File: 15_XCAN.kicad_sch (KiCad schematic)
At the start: 16 parts

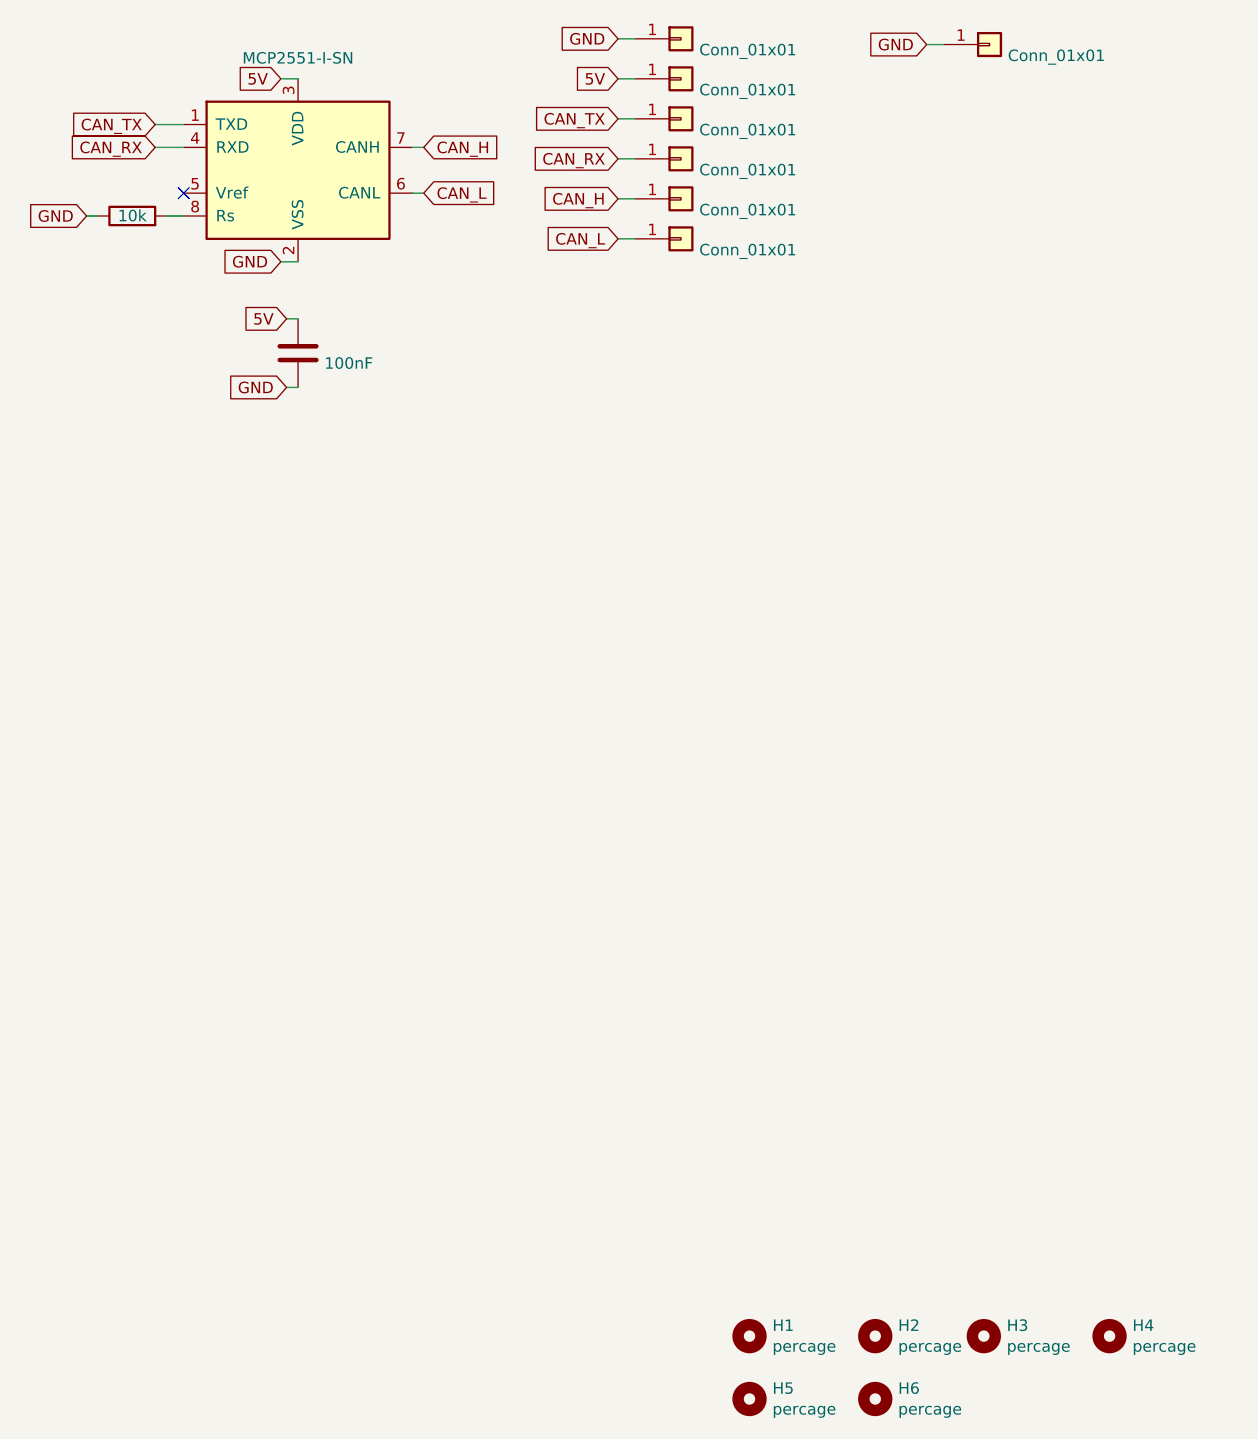
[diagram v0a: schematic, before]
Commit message: réduction de taille du pcb
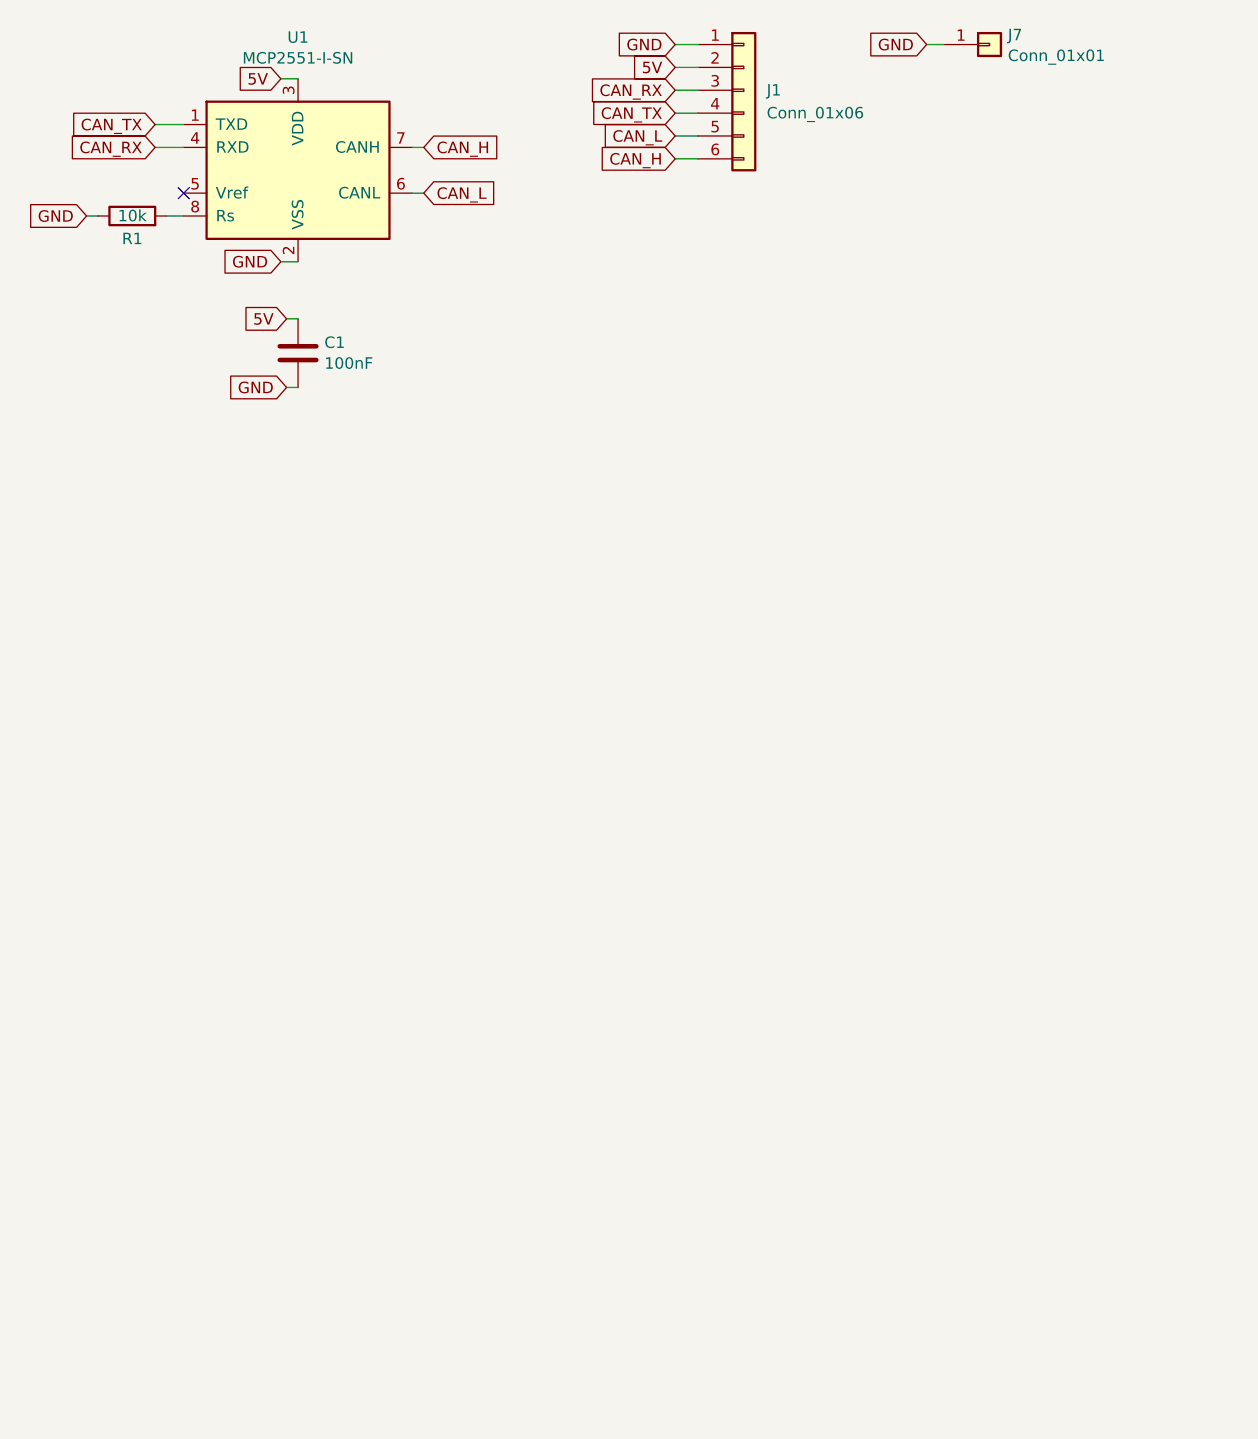
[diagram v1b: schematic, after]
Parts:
- removed ? (x6): Conn_01x01, Chimere_mods:Castellated_conn, symbol Connector_Generic:Conn_01x01
- removed H1, H2, H3, H4, H5, H6: percage, Chimere_comps:trou, symbol Mechanical:MountingHole
- added J1: Conn_01x06, Connector_PinHeader_2.54mm:PinHeader_1x06_P2.54mm_Vertical, symbol Connector_Generic:Conn_01x06
- J7: renamed from ?; footprint Chimere_mods:Castellated_conn -> Connector_PinHeader_2.54mm:PinHeader_1x01_P2.54mm_Vertical
- gave numbers to parts that had none: 3
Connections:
- net 5V: now also J1.2 (Pin_2)
- net CAN_H: now also J1.6 (Pin_6)
- net CAN_L: now also J1.5 (Pin_5)
- net CAN_RX: now also J1.3 (Pin_3)
- net CAN_TX: now also J1.4 (Pin_4)
- net GND: now also J1.1 (Pin_1)

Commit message: maj fichiers de fabrication
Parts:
- C1: LCSC (none) -> C14663
- U1: LCSC (none) -> C7376
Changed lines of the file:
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@@
       (effects (font (size 1.27 1.27) italic) hide)
     )
-    (property "Datasheet" "C7376" (id 3) (at 63.5 46.99 0)
+    (property "Datasheet" "-" (id 3) (at 63.5 46.99 0)
       (effects (font (size 1.27 1.27)) hide)
     )
+    (property "LCSC" "C7376" (id 4) (at 63.5 46.99 0))
     (pin "1")
     (pin "2")
@@
       (effects (font (size 1.27 1.27)) hide)
     )
-    (property "Datasheet" "C14663" (id 3) (at 63.5 67.31 0)
+    (property "Datasheet" "-" (id 3) (at 63.5 67.31 0)
       (effects (font (size 1.27 1.27)) hide)
     )
+    (property "LCSC" "C14663" (id 4) (at 63.5 67.31 0))
     (pin "1")
     (pin "2")

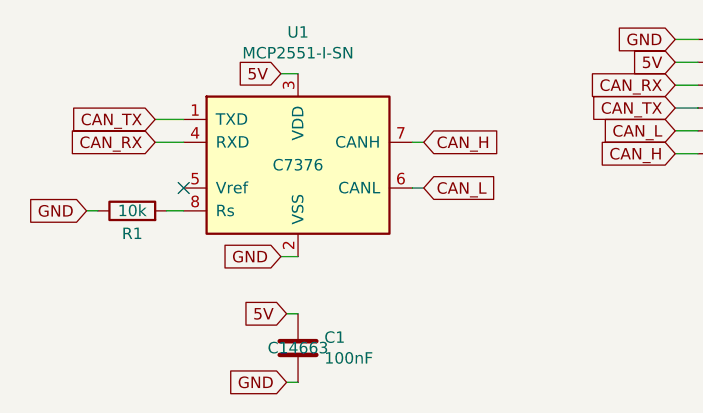
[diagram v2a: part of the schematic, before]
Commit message: maj
ajout sur silk
changement sourcing jlcpcb
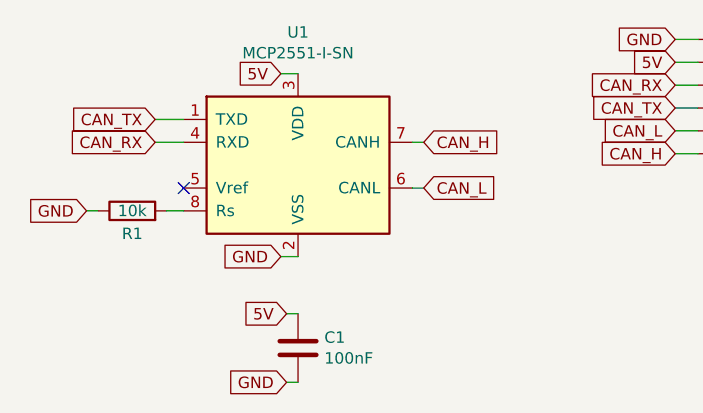
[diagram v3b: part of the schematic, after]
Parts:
- R1: LCSC (none) -> C25804
- U1: LCSC C7376 -> C49558
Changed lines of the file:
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@@
       (effects (font (size 1.27 1.27)) hide)
     )
-    (property "Datasheet" "C25804" (id 3) (at 45.085 52.07 0)
+    (property "Datasheet" "~" (id 3) (at 45.085 52.07 0)
+      (effects (font (size 1.27 1.27)) hide)
+    )
+    (property "LCSC" "C25804" (id 4) (at 45.085 52.07 90)
       (effects (font (size 1.27 1.27)) hide)
     )
@@
       (effects (font (size 1.27 1.27) italic) hide)
     )
-    (property "Datasheet" "-" (id 3) (at 63.5 46.99 0)
+    (property "Datasheet" "http://ww1.microchip.com/downloads/en/devicedoc/21667d.pdf" (id 3) (at 63.5 46.99 0)
       (effects (font (size 1.27 1.27)) hide)
     )
-    (property "LCSC" "C7376" (id 4) (at 63.5 46.99 0))
+    (property "LCSC" "C49558" (id 4) (at 63.5 46.99 0)
+      (effects (font (size 1.27 1.27)) hide)
+    )
     (pin "1")
     (pin "2")
@@
       (effects (font (size 1.27 1.27)) hide)
     )
-    (property "Datasheet" "-" (id 3) (at 63.5 67.31 0)
+    (property "Datasheet" "~" (id 3) (at 63.5 67.31 0)
       (effects (font (size 1.27 1.27)) hide)
     )
-    (property "LCSC" "C14663" (id 4) (at 63.5 67.31 0))
+    (property "LCSC" "C14663" (id 4) (at 63.5 67.31 0)
+      (effects (font (size 1.27 1.27)) hide)
+    )
     (pin "1")
     (pin "2")

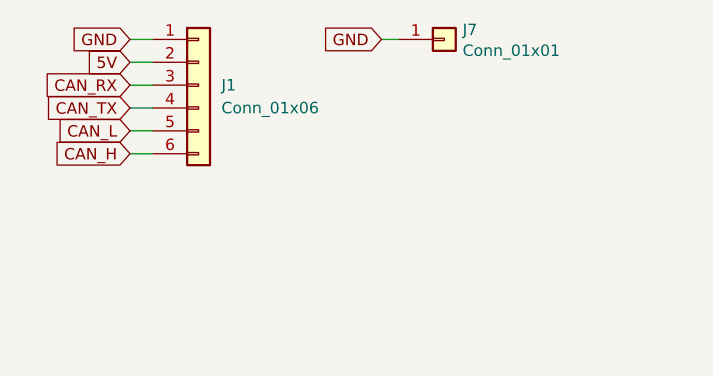
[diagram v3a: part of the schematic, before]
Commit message: version castellated holes
rajout des castellated holes
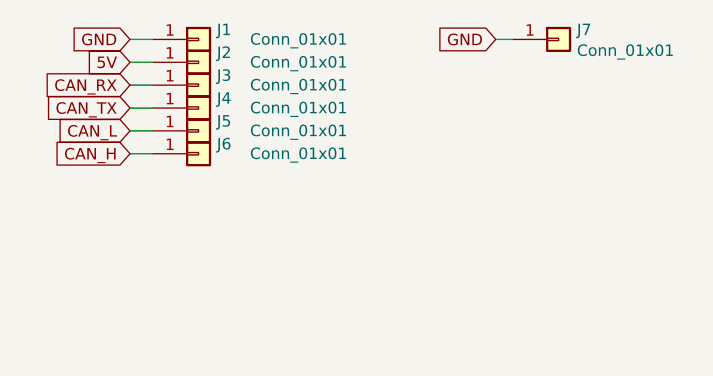
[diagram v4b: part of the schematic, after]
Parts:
- removed J1: Conn_01x06, Connector_PinHeader_2.54mm:PinHeader_1x06_P2.54mm_Vertical, symbol Connector_Generic:Conn_01x06
- added J1, J2, J3, J4, J5, J6: Conn_01x01, Chimere_mods:Castellated_conn, symbol Connector_Generic:Conn_01x01
- J7: footprint Connector_PinHeader_2.54mm:PinHeader_1x01_P2.54mm_Vertical -> Chimere_mods:Cast_co_1_905
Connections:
- net 5V: now also J2.1 (Pin_1)
- net CAN_H: now also J6.1 (Pin_1)
- net CAN_L: now also J5.1 (Pin_1)
- net CAN_RX: now also J3.1 (Pin_1)
- net CAN_TX: now also J4.1 (Pin_1)
- net GND: now also J1.1 (Pin_1)
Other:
- moved on the sheet: J7
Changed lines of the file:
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@@
     (stroke (width 0) (type default) (color 0 0 0 0))
   )
-  (wire (pts (xy 133.35 33.02) (xy 135.255 33.02))
+  (wire (pts (xy 146.05 33.02) (xy 147.955 33.02))
     (stroke (width 0) (type default) (color 0 0 0 0))
   )
@@
     )
   )
-  (global_label "GND" (shape input) (at 133.35 33.02 180) (fields_autoplaced)
-    (effects (font (size 1.27 1.27)) (justify right))
-    (property "Intersheet References" "${INTERSHEET_REFS}" (id 0) (at 0 0 0)
+  (global_label "GND" (shape input) (at 146.05 33.02 180) (fields_autoplaced)
+    (effects (font (size 1.27 1.27)) (justify right))
+    (property "Intersheet References" "${INTERSHEET_REFS}" (id 0) (at 12.7 0 0)
       (effects (font (size 1.27 1.27)) hide)
     )
@@
     (pin "2")
   )
-  (symbol (lib_id "Connector_Generic:Conn_01x01") (at 140.335 33.02 0) (unit 1)
-    (in_bom yes) (on_board yes)
-    (property "Reference" "J7" (id 0) (at 142.367 31.9532 0)
-      (effects (font (size 1.27 1.27)) (justify left))
-    )
-    (property "Value" "Conn_01x01" (id 1) (at 142.367 34.2646 0)
-      (effects (font (size 1.27 1.27)) (justify left))
-    )
-    (property "Footprint" "Connector_PinHeader_2.54mm:PinHeader_1x01_P2.54mm_Vertical" (id 2) (at 140.335 33.02 0)
-      (effects (font (size 1.27 1.27)) hide)
-    )
-    (property "Datasheet" "~" (id 3) (at 140.335 33.02 0)
-      (effects (font (size 1.27 1.27)) hide)
-    )
-    (pin "1")
-  )
-  (symbol (lib_id "Connector_Generic:Conn_01x06") (at 113.03 38.1 0) (unit 1)
-    (in_bom yes) (on_board yes) (fields_autoplaced)
-    (property "Reference" "J1" (id 0) (at 115.57 38.0999 0)
-      (effects (font (size 1.27 1.27)) (justify left))
-    )
-    (property "Value" "Conn_01x06" (id 1) (at 115.57 40.6399 0)
-      (effects (font (size 1.27 1.27)) (justify left))
-    )
-    (property "Footprint" "Connector_PinHeader_2.54mm:PinHeader_1x06_P2.54mm_Vertical" (id 2) (at 113.03 38.1 0)
+  (symbol (lib_id "Connector_Generic:Conn_01x01") (at 153.035 33.02 0) (unit 1)
+    (in_bom yes) (on_board yes)
+    (property "Reference" "J7" (id 0) (at 155.067 31.9532 0)
+      (effects (font (size 1.27 1.27)) (justify left))
+    )
+    (property "Value" "Conn_01x01" (id 1) (at 155.067 34.2646 0)
+      (effects (font (size 1.27 1.27)) (justify left))
+    )
+    (property "Footprint" "Chimere_mods:Cast_co_1_905" (id 2) (at 153.035 33.02 0)
+      (effects (font (size 1.27 1.27)) hide)
+    )
+    (property "Datasheet" "~" (id 3) (at 153.035 33.02 0)
+      (effects (font (size 1.27 1.27)) hide)
+    )
+    (pin "1")
+  )
+  (symbol (lib_id "Connector_Generic:Conn_01x01") (at 113.03 33.02 0) (unit 1)
+    (in_bom yes) (on_board yes)
+    (property "Reference" "J1" (id 0) (at 115.062 31.9532 0)
+      (effects (font (size 1.27 1.27)) (justify left))
+    )
+    (property "Value" "Conn_01x01" (id 1) (at 118.745 33.02 0)
+      (effects (font (size 1.27 1.27)) (justify left))
+    )
+    (property "Footprint" "Chimere_mods:Castellated_conn" (id 2) (at 113.03 33.02 0)
+      (effects (font (size 1.27 1.27)) hide)
+    )
+    (property "Datasheet" "~" (id 3) (at 113.03 33.02 0)
+      (effects (font (size 1.27 1.27)) hide)
+    )
+    (pin "1")
+  )
+  (symbol (lib_id "Connector_Generic:Conn_01x01") (at 113.03 45.72 0) (unit 1)
+    (in_bom yes) (on_board yes)
+    (property "Reference" "J6" (id 0) (at 115.062 44.6532 0)
+      (effects (font (size 1.27 1.27)) (justify left))
+    )
+    (property "Value" "Conn_01x01" (id 1) (at 118.745 45.72 0)
+      (effects (font (size 1.27 1.27)) (justify left))
+    )
+    (property "Footprint" "Chimere_mods:Castellated_conn" (id 2) (at 113.03 45.72 0)
+      (effects (font (size 1.27 1.27)) hide)
+    )
+    (property "Datasheet" "~" (id 3) (at 113.03 45.72 0)
+      (effects (font (size 1.27 1.27)) hide)
+    )
+    (pin "1")
+  )
+  (symbol (lib_id "Connector_Generic:Conn_01x01") (at 113.03 35.56 0) (unit 1)
+    (in_bom yes) (on_board yes)
+    (property "Reference" "J2" (id 0) (at 115.062 34.4932 0)
+      (effects (font (size 1.27 1.27)) (justify left))
+    )
+    (property "Value" "Conn_01x01" (id 1) (at 118.745 35.56 0)
+      (effects (font (size 1.27 1.27)) (justify left))
+    )
+    (property "Footprint" "Chimere_mods:Castellated_conn" (id 2) (at 113.03 35.56 0)
+      (effects (font (size 1.27 1.27)) hide)
+    )
+    (property "Datasheet" "~" (id 3) (at 113.03 35.56 0)
+      (effects (font (size 1.27 1.27)) hide)
+    )
+    (pin "1")
+  )
+  (symbol (lib_id "Connector_Generic:Conn_01x01") (at 113.03 40.64 0) (unit 1)
+    (in_bom yes) (on_board yes)
+    (property "Reference" "J4" (id 0) (at 115.062 39.5732 0)
+      (effects (font (size 1.27 1.27)) (justify left))
+    )
+    (property "Value" "Conn_01x01" (id 1) (at 118.745 40.64 0)
+      (effects (font (size 1.27 1.27)) (justify left))
+    )
+    (property "Footprint" "Chimere_mods:Castellated_conn" (id 2) (at 113.03 40.64 0)
+      (effects (font (size 1.27 1.27)) hide)
+    )
+    (property "Datasheet" "~" (id 3) (at 113.03 40.64 0)
+      (effects (font (size 1.27 1.27)) hide)
+    )
+    (pin "1")
+  )
+  (symbol (lib_id "Connector_Generic:Conn_01x01") (at 113.03 38.1 0) (unit 1)
+    (in_bom yes) (on_board yes)
+    (property "Reference" "J3" (id 0) (at 115.062 37.0332 0)
+      (effects (font (size 1.27 1.27)) (justify left))
+    )
+    (property "Value" "Conn_01x01" (id 1) (at 118.745 38.1 0)
+      (effects (font (size 1.27 1.27)) (justify left))
+    )
+    (property "Footprint" "Chimere_mods:Castellated_conn" (id 2) (at 113.03 38.1 0)
       (effects (font (size 1.27 1.27)) hide)
     )
@@
     )
     (pin "1")
-    (pin "2")
-    (pin "3")
-    (pin "4")
-    (pin "5")
-    (pin "6")
+  )
+  (symbol (lib_id "Connector_Generic:Conn_01x01") (at 113.03 43.18 0) (unit 1)
+    (in_bom yes) (on_board yes)
+    (property "Reference" "J5" (id 0) (at 115.062 42.1132 0)
+      (effects (font (size 1.27 1.27)) (justify left))
+    )
+    (property "Value" "Conn_01x01" (id 1) (at 118.745 43.18 0)
+      (effects (font (size 1.27 1.27)) (justify left))
+    )
+    (property "Footprint" "Chimere_mods:Castellated_conn" (id 2) (at 113.03 43.18 0)
+      (effects (font (size 1.27 1.27)) hide)
+    )
+    (property "Datasheet" "~" (id 3) (at 113.03 43.18 0)
+      (effects (font (size 1.27 1.27)) hide)
+    )
+    (pin "1")
   )
   (sheet_instances
@@
       (reference "C1") (unit 1) (value "100nF") (footprint "Capacitor_SMD:C_0603_1608Metric")
     )
-    (path "/a074e81a-dbd6-446d-bb18-31b0c201fb6d"
-      (reference "J1") (unit 1) (value "Conn_01x06") (footprint "Connector_PinHeader_2.54mm:PinHeader_1x06_P2.54mm_Vertical")
+    (path "/53ba31da-d311-46aa-83e3-50cf68403b33"
+      (reference "J1") (unit 1) (value "Conn_01x01") (footprint "Chimere_mods:Castellated_conn")
+    )
+    (path "/96511534-681c-4fd9-aa6e-81899ccb0142"
+      (reference "J2") (unit 1) (value "Conn_01x01") (footprint "Chimere_mods:Castellated_conn")
+    )
+    (path "/bbd3c7ad-f3fc-45d4-9d1c-5d8c621ee1f4"
+      (reference "J3") (unit 1) (value "Conn_01x01") (footprint "Chimere_mods:Castellated_conn")
+    )
+    (path "/9ddfe612-6d95-4ee7-bb18-547475ab9e51"
+      (reference "J4") (unit 1) (value "Conn_01x01") (footprint "Chimere_mods:Castellated_conn")
+    )
+    (path "/f2000fcd-8b19-480f-a414-bad08e21a88f"
+      (reference "J5") (unit 1) (value "Conn_01x01") (footprint "Chimere_mods:Castellated_conn")
+    )
+    (path "/887289a8-57cc-4129-80ed-109079be6297"
+      (reference "J6") (unit 1) (value "Conn_01x01") (footprint "Chimere_mods:Castellated_conn")
     )
     (path "/00000000-0000-0000-0000-000060afa160"
-      (reference "J7") (unit 1) (value "Conn_01x01") (footprint "Connector_PinHeader_2.54mm:PinHeader_1x01_P2.54mm_Vertical")
+      (reference "J7") (unit 1) (value "Conn_01x01") (footprint "Chimere_mods:Cast_co_1_905")
     )
     (path "/00000000-0000-0000-0000-000060784930"
